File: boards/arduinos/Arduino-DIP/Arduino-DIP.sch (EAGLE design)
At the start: 16 parts, among them IC1 ATMEGA 328, IC2 MCP1702-33, X1 16 MHz

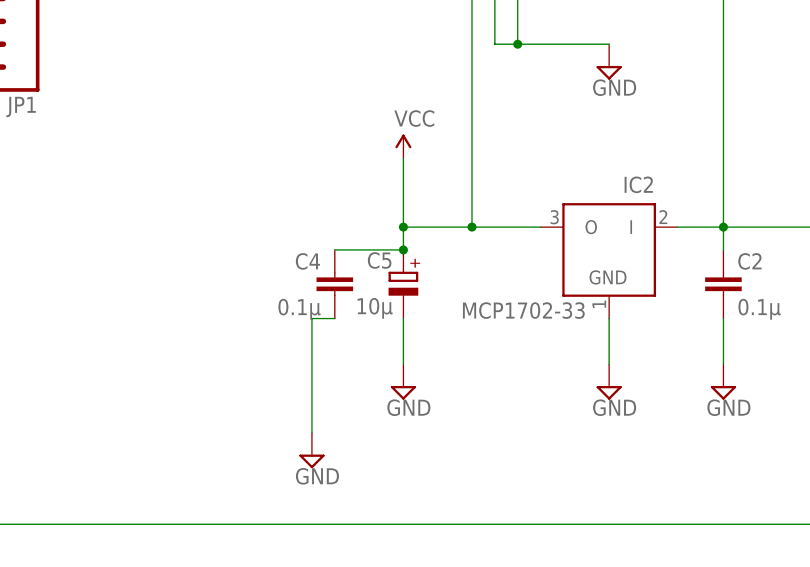
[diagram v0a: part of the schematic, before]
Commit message: updated radio with better regulator
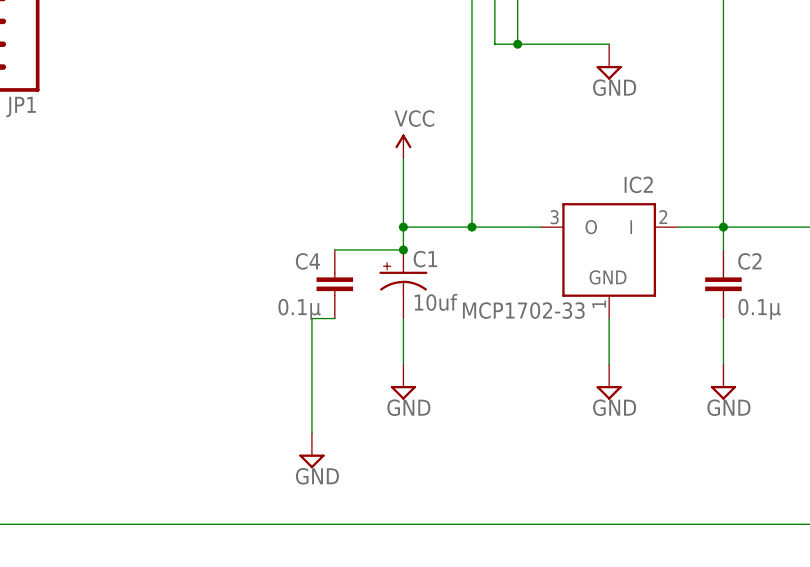
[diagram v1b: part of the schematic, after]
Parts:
- removed C5: 10µ, resistor:CPOL-EUE1.8-4
- added C1: 10uf, SparkFun-Capacitors:CAP_POLPTH2
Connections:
- net GND: now also C1.-; no longer C5.-
- net VCC: now also C1.+; no longer C5.+
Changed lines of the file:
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@@
 <part name="SUPPLY9" library="supply2" deviceset="GND" device=""/>
 <part name="IC2" library="JeeLabs" deviceset="MCP1702" device="Z" value="MCP1702-33"/>
-<part name="C5" library="resistor" deviceset="CPOL-EU" device="E1.8-4" value="10µ"/>
 <part name="C2" library="resistor" deviceset="C-EU" device="025-024X044" value="0.1µ"/>
 <part name="SUPPLY10" library="supply2" deviceset="GND" device=""/>
@@
 <part name="JP7" library="SparkFun-Connectors" deviceset="M04" device="PTH"/>
 <part name="JP5" library="SparkFun-Connectors" deviceset="M06" device="NO_SILK"/>
+<part name="C1" library="SparkFun-Capacitors" deviceset="CAP_POL" device="PTH2" value="10uf"/>
 </parts>
 <sheets>
@@
 <instance part="SUPPLY9" gate="GND" x="53.34" y="20.32"/>
 <instance part="IC2" gate="G$1" x="210.82" y="60.96" rot="MR0"/>
-<instance part="C5" gate="G$1" x="187.96" y="58.42" rot="MR0"/>
 <instance part="C2" gate="G$1" x="223.52" y="58.42"/>
 <instance part="SUPPLY10" gate="GND" x="177.8" y="38.1"/>
@@
 <instance part="JP7" gate="G$1" x="198.12" y="93.98" rot="R270"/>
 <instance part="JP5" gate="G$1" x="43.18" y="30.48"/>
+<instance part="C1" gate="G$1" x="187.96" y="58.42"/>
 </instances>
 <busses>
@@
 </segment>
 <segment>
-<pinref part="C5" gate="G$1" pin="-"/>
 <pinref part="SUPPLY11" gate="GND" pin="GND"/>
 <wire x1="187.96" y1="48.26" x2="187.96" y2="53.34" width="0.1524" layer="91"/>
+<pinref part="C1" gate="G$1" pin="-"/>
 </segment>
 <segment>
@@
 <wire x1="195.58" y1="63.5" x2="203.2" y2="63.5" width="0.1524" layer="91"/>
 <wire x1="187.96" y1="71.12" x2="187.96" y2="63.5" width="0.1524" layer="91"/>
-<pinref part="C5" gate="G$1" pin="+"/>
 <pinref part="C4" gate="G$1" pin="1"/>
 <wire x1="187.96" y1="60.96" x2="180.34" y2="60.96" width="0.1524" layer="91"/>
 <wire x1="187.96" y1="63.5" x2="187.96" y2="60.96" width="0.1524" layer="91"/>
 <junction x="187.96" y="63.5"/>
-<junction x="187.96" y="60.96"/>
 <wire x1="195.58" y1="88.9" x2="195.58" y2="63.5" width="0.1524" layer="91"/>
 <junction x="195.58" y="63.5"/>
 <pinref part="JP7" gate="G$1" pin="1"/>
-</segment>
-<segment>
+<pinref part="C1" gate="G$1" pin="+"/>
+<junction x="187.96" y="60.96"/>
+</segment>
+<segment>
